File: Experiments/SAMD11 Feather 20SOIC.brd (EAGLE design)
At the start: 50.8 x 22.9 mm, 30 parts, among them IC1 ATSAMD11D14A-SSNT, J1 10118193-0001LF, Q1 DMG341, SW1 SPST_TACT-KMR2, U1 AP2112-3.3, U2 MCP73831T-2ACI/OT, X1 JSTPH, X2 2x5 0.05" SWD

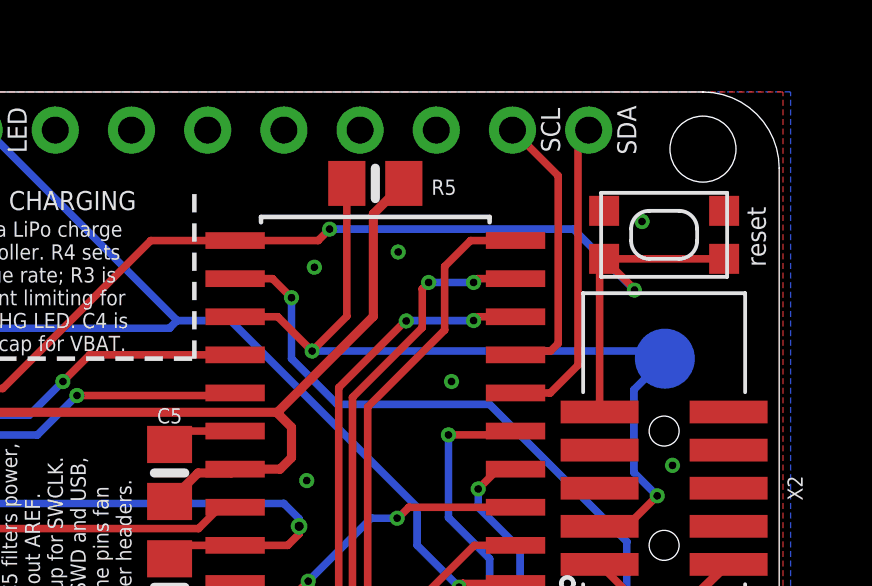
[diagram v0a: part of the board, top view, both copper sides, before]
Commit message: unswap swdio and swclk pins
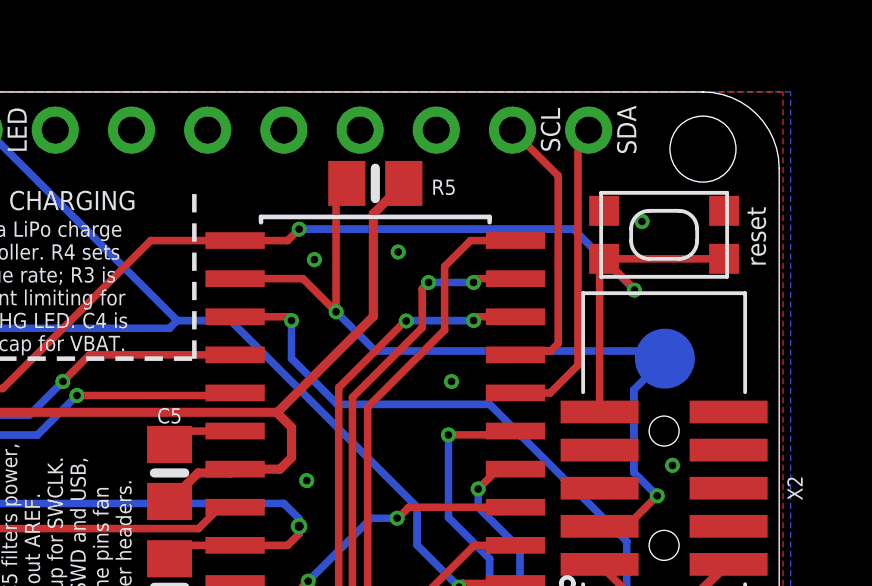
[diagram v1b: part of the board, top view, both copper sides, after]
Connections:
- net SWCLK: now also IC1.12; no longer IC1.13
- net SWDIO: now also IC1.13; no longer IC1.12
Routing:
- net SWCLK: track 28.6 -> 27.5 mm
- net SWDIO: track 22.6 -> 21.7 mm
